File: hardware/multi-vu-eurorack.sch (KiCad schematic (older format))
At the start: 77 parts, among them IC1 LM4040DBZ-10, IC2 ATtiny85, IC3 74HC595, IC4 74HC595, J1 EURO_HEADER_10pin, J2 AVR-ISP-6, SW1 EVQQ2, U1 TLV172IDCK, U2 TL074, U3 L78L05_SOT89, U4 MCP6001-OT

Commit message: Added input and output jacks and a larger array of LEDs for the main panel.
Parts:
- added D10, D24, D25, D26, D40, D41, D42, D8, D9: Y, LED_SMD:LED_0603_1608Metric_Pad1.05x0.95mm_HandSolder, symbol Device:LED_Small_ALT
- added D11, D12, D13, D14, D15, D16, D27, D28, D29, D30, D31, D32, D43, D44, D45, D46, D47, D48: G, LED_SMD:LED_0603_1608Metric_Pad1.05x0.95mm_HandSolder, symbol Device:LED_Small_ALT
- added D17, D18, D33, D34, D49, D50: B, LED_SMD:LED_0603_1608Metric_Pad1.05x0.95mm_HandSolder, symbol Device:LED_Small_ALT
- added D19, D20, D3, D35, D36, D4: R, LED_SMD:LED_0603_1608Metric_Pad1.05x0.95mm_HandSolder, symbol Device:LED_Small_ALT
- added D21, D22, D23, D37, D38, D39, D5, D6, D7: A, LED_SMD:LED_0603_1608Metric_Pad1.05x0.95mm_HandSolder, symbol Device:LED_Small_ALT
- added J1, J4, J5, J6, J7: AudioJack2_SwitchT, Connector_Audio:Jack_3.5mm_QingPu_WQP-PJ398SM_Vertical_CircularHoles, symbol Connector:AudioJack2_SwitchT
- D51: renamed from D3; value LED_Small_ALT -> R
- D52: renamed from D4; value LED_Small_ALT -> R
- D53: renamed from D5; value LED_Small_ALT -> A
- D54: renamed from D6; value LED_Small_ALT -> A
- D55: renamed from D7; value LED_Small_ALT -> A
- D56: renamed from D8; value LED_Small_ALT -> Y
- D57: renamed from D9; value LED_Small_ALT -> Y
- D58: renamed from D10; value LED_Small_ALT -> Y
- D59: renamed from D11; value LED_Small_ALT -> G
- D60: renamed from D12; value LED_Small_ALT -> G
- D61: renamed from D13; value LED_Small_ALT -> G
- D62: renamed from D14; value LED_Small_ALT -> G
- D63: renamed from D15; value LED_Small_ALT -> G
- D64: renamed from D16; value LED_Small_ALT -> G
- D65: renamed from D17; value LED_Small_ALT -> B
- D66: renamed from D18; value LED_Small_ALT -> B
- renumbered C9 to C1, C13 to C10, C15 to C11, C4 to C12, C5 to C13, C6 to C14, C7 to C15, C11 to C16, C20 to C17, C14 to C18, C21 to C19, C10 to C2, C22 to C20, C16 to C21, C17 to C22, C1 to C3, C2 to C4, C3 to C5, C8 to C6, C18 to C7, C19 to C8, C12 to C9, J1 to J2, J2 to J3, R3 to R1, R14 to R10, R15 to R11, R8 to R12, R9 to R13, R16 to R14, R17 to R15, R12 to R16, R18 to R17, R19 to R18, R13 to R19, R4 to R2, R6 to R3, R7 to R4, R1 to R5, R10 to R6, R11 to R7, R2 to R8, R5 to R9, U2 to U1, U1 to U2, U4 to U3, U3 to U4
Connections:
- net INPUT is gone; now on net GND: R5.2
- net GND: now also J1.S, J1.T, J1.TN, J4.S, J4.TN, J5.S, J5.TN, J6.S, J6.TN, J7.S, J7.TN
- net OUTA: now also J4.T
- net OUTB: now also J6.T
- net OUTC: now also J5.T
- net OUTD: now also J7.T
- net at IC3.1 (QB): now also D4.2 (A); no longer D52.2 (A)
- net at IC3.15 (QA): now also D3.2 (A); no longer D51.2 (A)
- net at IC3.2 (QC): now also D5.2 (A); no longer D53.2 (A)
- net at IC3.3 (QD): now also D6.2 (A); no longer D54.2 (A)
- net at IC3.4 (QE): now also D7.2 (A); no longer D55.2 (A)
- net at IC3.5 (QF): now also D8.2 (A); no longer D56.2 (A)
- net at IC3.6 (QG): now also D9.2 (A); no longer D57.2 (A)
- net at IC3.7 (QH): now also D10.2 (A); no longer D58.2 (A)
- net at IC4.1 (QB): now also D12.2 (A); no longer D60.2 (A)
- net at IC4.15 (QA): now also D11.2 (A); no longer D59.2 (A)
- net at IC4.2 (QC): now also D13.2 (A); no longer D61.2 (A)
- net at IC4.3 (QD): now also D14.2 (A); no longer D62.2 (A)
- net at IC4.4 (QE): now also D15.2 (A); no longer D63.2 (A)
- net at IC4.5 (QF): now also D16.2 (A); no longer D64.2 (A)
- net at IC4.6 (QG): now also D17.2 (A); no longer D65.2 (A)
- net at IC4.7 (QH): now also D18.2 (A); no longer D66.2 (A)
- new net: D43.1 (K), D59.2 (A)
- new net: D44.1 (K), D60.2 (A)
- new net: D45.1 (K), D61.2 (A)
- new net: D46.1 (K), D62.2 (A)
- new net: D47.1 (K), D63.2 (A)
- new net: D48.1 (K), D64.2 (A)
- new net: D49.1 (K), D65.2 (A)
- new net: D50.1 (K), D66.2 (A)
- new net: D28.1 (K), D44.2 (A)
- new net: D29.1 (K), D45.2 (A)
- new net: D30.1 (K), D46.2 (A)
- new net: D31.1 (K), D47.2 (A)
- new net: D32.1 (K), D48.2 (A)
- new net: D33.1 (K), D49.2 (A)
- new net: D34.1 (K), D50.2 (A)
- new net: D27.1 (K), D43.2 (A)
- new net: D36.1 (K), D52.2 (A)
- new net: D20.1 (K), D36.2 (A)
- new net: D37.1 (K), D53.2 (A)
- new net: D21.1 (K), D37.2 (A)
- new net: D38.1 (K), D54.2 (A)
- new net: D22.1 (K), D38.2 (A)
- new net: D39.1 (K), D55.2 (A)
- new net: D23.1 (K), D39.2 (A)
- new net: D40.1 (K), D56.2 (A)
- new net: D24.1 (K), D40.2 (A)
- new net: D41.1 (K), D57.2 (A)
- new net: D25.1 (K), D41.2 (A)
- new net: D42.1 (K), D58.2 (A)
- new net: D26.1 (K), D42.2 (A)
- new net: D35.1 (K), D51.2 (A)
- new net: D19.1 (K), D35.2 (A)
- new net: D12.1 (K), D28.2 (A)
- new net: D13.1 (K), D29.2 (A)
- new net: D14.1 (K), D30.2 (A)
- new net: D15.1 (K), D31.2 (A)
- new net: D16.1 (K), D32.2 (A)
- new net: D17.1 (K), D33.2 (A)
- new net: D18.1 (K), D34.2 (A)
- new net: D11.1 (K), D27.2 (A)
- new net: D20.2 (A), D4.1 (K)
- new net: D21.2 (A), D5.1 (K)
- new net: D22.2 (A), D6.1 (K)
- new net: D23.2 (A), D7.1 (K)
- new net: D24.2 (A), D8.1 (K)
- new net: D25.2 (A), D9.1 (K)
- new net: D10.1 (K), D26.2 (A)
- new net: D19.2 (A), D3.1 (K)
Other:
- moved on the sheet: C1, C10, C11, C12, C13, C14, C15, C16, C17, C18, C19, C2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

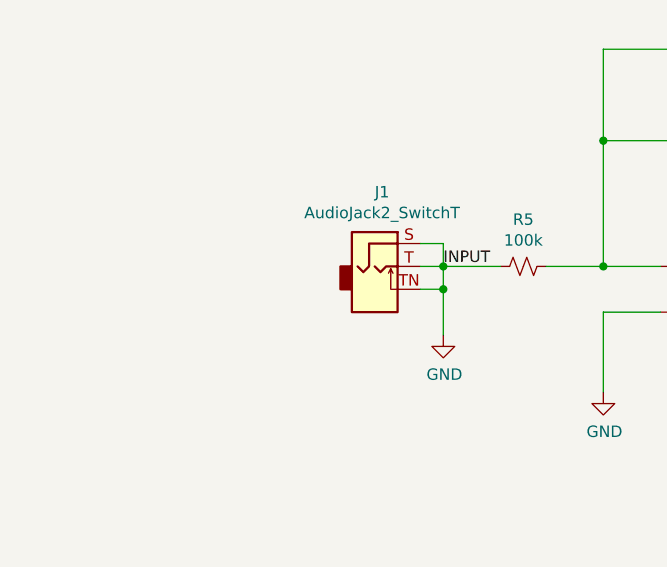
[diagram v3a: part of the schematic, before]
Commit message: Updated netlist to include audio jacks. Corrected some small connection issues.
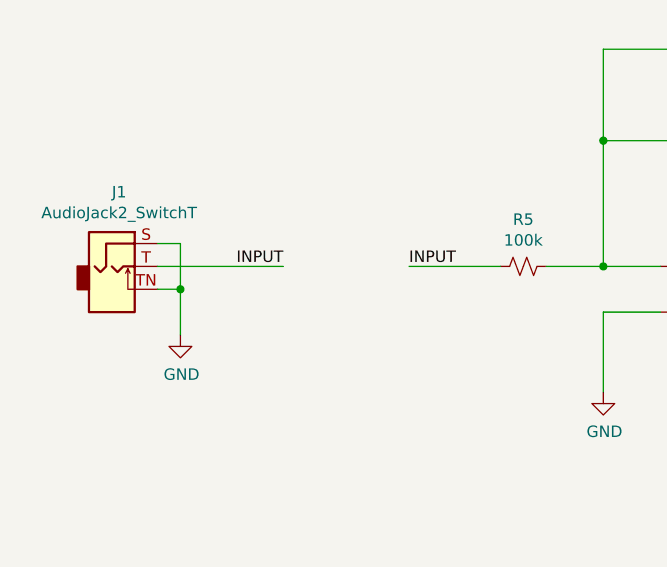
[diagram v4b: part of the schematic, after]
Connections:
- net GND: no longer J1.T, R5.2
- new net INPUT: J1.T, R5.2
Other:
- moved on the sheet: J1
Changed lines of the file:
@@
 Text Label 5100 4400 2    50   ~ 0
 MULT_INPUT
-Text Label 2700 3250 0    50   ~ 0
+Text Label 2000 3250 2    50   ~ 0
 INPUT
 Wire Wire Line
@@
 L Connector:AudioJack2_SwitchT J1
 U 1 1 60D7F728
-P 2400 3250
-F 0 "J1" H 2432 3575 50  0000 C CNN
-F 1 "AudioJack2_SwitchT" H 2432 3484 50  0000 C CNN
-F 2 "Connector_Audio:Jack_3.5mm_QingPu_WQP-PJ398SM_Vertical_CircularHoles" H 2400 3250 50  0001 C CNN
-F 3 "~" H 2400 3250 50  0001 C CNN
-	1    2400 3250
-	1    0    0    -1
-$EndComp
-Wire Wire Line
-	2600 3250 2700 3250
-Wire Wire Line
-	2600 3150 2700 3150
-Wire Wire Line
-	2700 3150 2700 3250
-Connection ~ 2700 3250
-Wire Wire Line
-	2700 3250 2950 3250
-Wire Wire Line
-	2700 3250 2700 3350
-Wire Wire Line
-	2600 3350 2700 3350
-Connection ~ 2700 3350
-Wire Wire Line
-	2700 3350 2700 3550
+P 1250 3250
+F 0 "J1" H 1282 3575 50  0000 C CNN
+F 1 "AudioJack2_SwitchT" H 1282 3484 50  0000 C CNN
+F 2 "Connector_Audio:Jack_3.5mm_QingPu_WQP-PJ398SM_Vertical_CircularHoles" H 1250 3250 50  0001 C CNN
+F 3 "~" H 1250 3250 50  0001 C CNN
+	1    1250 3250
+	1    0    0    -1
+$EndComp
+Wire Wire Line
+	1450 3150 1550 3150
+Wire Wire Line
+	1450 3350 1550 3350
+Wire Wire Line
+	1550 3350 1550 3550
 $Comp
 L 4ms-power:GND #PWR03
 U 1 1 60E2588D
-P 2700 3550
-F 0 "#PWR03" H 2700 3300 50  0001 C CNN
-F 1 "GND" H 2705 3377 50  0000 C CNN
-F 2 "" H 2700 3550 50  0001 C CNN
-F 3 "" H 2700 3550 50  0001 C CNN
-	1    2700 3550
-	1    0    0    -1
-$EndComp
+P 1550 3550
+F 0 "#PWR03" H 1550 3300 50  0001 C CNN
+F 1 "GND" H 1555 3377 50  0000 C CNN
+F 2 "" H 1550 3550 50  0001 C CNN
+F 3 "" H 1550 3550 50  0001 C CNN
+	1    1550 3550
+	1    0    0    -1
+$EndComp
+Wire Wire Line
+	1450 3250 2000 3250
+Wire Wire Line
+	1550 3350 1550 3150
+Connection ~ 1550 3350
+Wire Wire Line
+	2950 3250 2550 3250
+Text Label 2550 3250 0    50   ~ 0
+INPUT
 $EndSCHEMATC

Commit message: Separated and arranged passives around mainboard ICs, started arranging LEDs on panel reverse.
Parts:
- IC3, IC4: footprint Package_SO:TSSOP-14_4.4x5mm_P0.65mm -> Package_SO:TSSOP-16_4.4x5mm_P0.65mm
- SW1: symbol Switch:SW_DPST -> Switch:SW_Push
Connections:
- net +5V: now also R23.2, R24.2; no longer R23.1, R24.1
- net GND: no longer SW1.3
- net at C11.2, IC2.1 (PB5/RESET), J3.5 (~RST)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: no longer SW1.4
- net at IC3.10 (~SRCLR): now also R23.1; no longer R23.2
- net at IC4.10 (~SRCLR): now also R24.1; no longer R24.2
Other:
- note added: "TODO: Add stacking header pins\nto connect the mainboard to the light board (i.e. the\nback of the control panel…)"
- moved on the sheet: R23, R24
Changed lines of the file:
@@
 F 0 "IC3" H 11050 3050 50  0000 C CNN
 F 1 "74HC595" H 11250 2450 50  0000 C CNN
-F 2 "Package_SO:TSSOP-14_4.4x5mm_P0.65mm" H 11050 3100 50  0001 C CNN
+F 2 "Package_SO:TSSOP-16_4.4x5mm_P0.65mm" H 11050 3100 50  0001 C CNN
 F 3 "http://www.ti.com/lit/ds/symlink/sn74hc595.pdf" H 11050 3100 50  0001 C CNN
 	1    11050 3100
@@
 F 0 "IC4" H 11050 5250 50  0000 C CNN
 F 1 "74HC595" H 11250 4650 50  0000 C CNN
-F 2 "Package_SO:TSSOP-14_4.4x5mm_P0.65mm" H 11050 5300 50  0001 C CNN
+F 2 "Package_SO:TSSOP-16_4.4x5mm_P0.65mm" H 11050 5300 50  0001 C CNN
 F 3 "http://www.ti.com/lit/ds/symlink/sn74hc595.pdf" H 11050 5300 50  0001 C CNN
 	1    11050 5300
@@
 $EndComp
 $Comp
-L Switch:SW_DPST SW1
+L Switch:SW_Push SW1
 U 1 1 60741EC8
-P 7650 3050
-F 0 "SW1" H 7650 3375 50  0000 C CNN
-F 1 "EVQQ2" H 7650 3284 50  0000 C CNN
-F 2 "Button_Switch_SMD:SW_SPST_EVQQ2" H 7650 3050 50  0001 C CNN
-F 3 "~" H 7650 3050 50  0001 C CNN
-	1    7650 3050
+P 7650 2950
+F 0 "SW1" H 7650 3275 50  0000 C CNN
+F 1 "EVQQ2" H 7650 3184 50  0000 C CNN
+F 2 "Button_Switch_SMD:SW_SPST_EVQQ2" H 7650 2950 50  0001 C CNN
+F 3 "~" H 7650 2950 50  0001 C CNN
+	1    7650 2950
 	1    0    0    -1
 $EndComp
@@
 	7350 3400 7350 3350
 Wire Wire Line
-	7350 3350 7350 3150
-Wire Wire Line
 	7350 2950 7450 2950
 Connection ~ 7350 3350
 Wire Wire Line
-	7450 3150 7350 3150
-Connection ~ 7350 3150
-Wire Wire Line
-	7350 3150 7350 2950
-Wire Wire Line
 	7850 2950 7950 2950
-Wire Wire Line
-	7850 3150 7950 3150
 Wire Wire Line
 	7950 3150 7950 2950
@@
 	10400 5100 10650 5100
 Wire Wire Line
-	10500 5200 10500 4600
-Wire Wire Line
-	10500 4600 10700 4600
+	10500 5200 10500 4800
 Wire Wire Line
 	10500 5200 10650 5200
@@
 	11050 4600 11050 4550
 Wire Wire Line
-	10350 3000 10350 2400
-Wire Wire Line
-	10350 2400 10600 2400
+	10350 3000 10350 2550
 Wire Wire Line
 	10350 3000 10650 3000
@@
 	0    1    1    0
 $EndComp
-$Comp
-L Device:R_Small_US R14
-U 1 1 607A8663
-P 6200 6100
-F 0 "R14" V 6150 5950 50  0000 C CNN
-F 1 "100k" V 6250 6300 50  0000 C CNN
-F 2 "Capacitor_SMD:C_0603_1608Metric_Pad1.05x0.95mm_HandSolder" H 6200 6100 50  0001 C CNN
-F 3 "~" H 6200 6100 50  0001 C CNN
-	1    6200 6100
-	0    1    1    0
-$EndComp
 Wire Wire Line
 	5800 6100 6100 6100
@@
 L Device:R_Small_US R23
 U 1 1 607B166F
-P 10700 2400
-F 0 "R23" V 10750 2500 50  0000 L CNN
-F 1 "10k" V 10650 2200 50  0000 L CNN
-F 2 "Capacitor_SMD:C_0603_1608Metric_Pad1.05x0.95mm_HandSolder" H 10700 2400 50  0001 C CNN
-F 3 "~" H 10700 2400 50  0001 C CNN
-	1    10700 2400
-	0    1    1    0
-$EndComp
-Wire Wire Line
-	10800 2400 11050 2400
+P 10350 2450
+F 0 "R23" V 10400 2550 50  0000 L CNN
+F 1 "10k" V 10300 2250 50  0000 L CNN
+F 2 "Capacitor_SMD:C_0603_1608Metric_Pad1.05x0.95mm_HandSolder" H 10350 2450 50  0001 C CNN
+F 3 "~" H 10350 2450 50  0001 C CNN
+	1    10350 2450
+	-1   0    0    1
+$EndComp
 $Comp
 L Device:R_Small_US R24
 U 1 1 607B2148
-P 10800 4600
-F 0 "R24" V 10868 4646 50  0000 L CNN
-F 1 "10k" V 10700 4550 50  0000 L CNN
-F 2 "Capacitor_SMD:C_0603_1608Metric_Pad1.05x0.95mm_HandSolder" H 10800 4600 50  0001 C CNN
-F 3 "~" H 10800 4600 50  0001 C CNN
-	1    10800 4600
-	0    1    1    0
-$EndComp
-Wire Wire Line
-	10900 4600 11050 4600
+P 10500 4700
+F 0 "R24" V 10568 4746 50  0000 L CNN
+F 1 "10k" V 10400 4650 50  0000 L CNN
+F 2 "Capacitor_SMD:C_0603_1608Metric_Pad1.05x0.95mm_HandSolder" H 10500 4700 50  0001 C CNN
+F 3 "~" H 10500 4700 50  0001 C CNN
+	1    10500 4700
+	-1   0    0    1
+$EndComp
 $Comp
 L 4ms-passives:C_Small C1
@@
 Text Label 2550 3250 0    50   ~ 0
 INPUT
+$Comp
+L Device:R_Small_US R14
+U 1 1 608209A8
+P 6200 6100
+F 0 "R14" V 6100 5950 50  0000 C CNN
+F 1 "100k" V 6300 6300 50  0000 C CNN
+F 2 "Capacitor_SMD:C_0603_1608Metric_Pad1.05x0.95mm_HandSolder" H 6200 6100 50  0001 C CNN
+F 3 "~" H 6200 6100 50  0001 C CNN
+	1    6200 6100
+	0    1    1    0
+$EndComp
+$Comp
+L power:+5V #PWR0101
+U 1 1 608C6683
+P 10500 4500
+F 0 "#PWR0101" H 10500 4350 50  0001 C CNN
+F 1 "+5V" H 10515 4673 50  0000 C CNN
+F 2 "" H 10500 4500 50  0001 C CNN
+F 3 "" H 10500 4500 50  0001 C CNN
+	1    10500 4500
+	1    0    0    -1
+$EndComp
+Wire Wire Line
+	10500 4500 10500 4600
+$Comp
+L power:+5V #PWR0102
+U 1 1 609E4F8E
+P 10350 2250
+F 0 "#PWR0102" H 10350 2100 50  0001 C CNN
+F 1 "+5V" H 10365 2423 50  0000 C CNN
+F 2 "" H 10350 2250 50  0001 C CNN
+F 3 "" H 10350 2250 50  0001 C CNN
+	1    10350 2250
+	1    0    0    -1
+$EndComp
+Wire Wire Line
+	10350 2250 10350 2350
+Wire Wire Line
+	7350 2950 7350 3350
+Text Notes 11950 2400 0    50   ~ 0
+TODO:  Add stacking header pins\nto connect the mainboard to the light board (i.e. the\nback of the control panel…)
+Text Notes 12050 4650 0    50   ~ 0
+TODO:  Add stacking header pins\nto connect the mainboard to the light board (i.e. the\nback of the control panel…)
 $EndSCHEMATC
